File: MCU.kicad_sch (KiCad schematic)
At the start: 83 parts, among them J1 Conn_01x02_Pin, J11 Logger Connector, J12 UART Connector, J13 External UART, J14 External I2C, J15 JTAG Header, J2 Conn_01x02_Pin, J27 Conn_01x02_Pin, SW1 XRSn_button, U13 M24M01E-FMN6TP, U17 TRS3221EIPWR, U5 F280025PNS, Y2 H130B-16.000-18-3030-EXT-TR

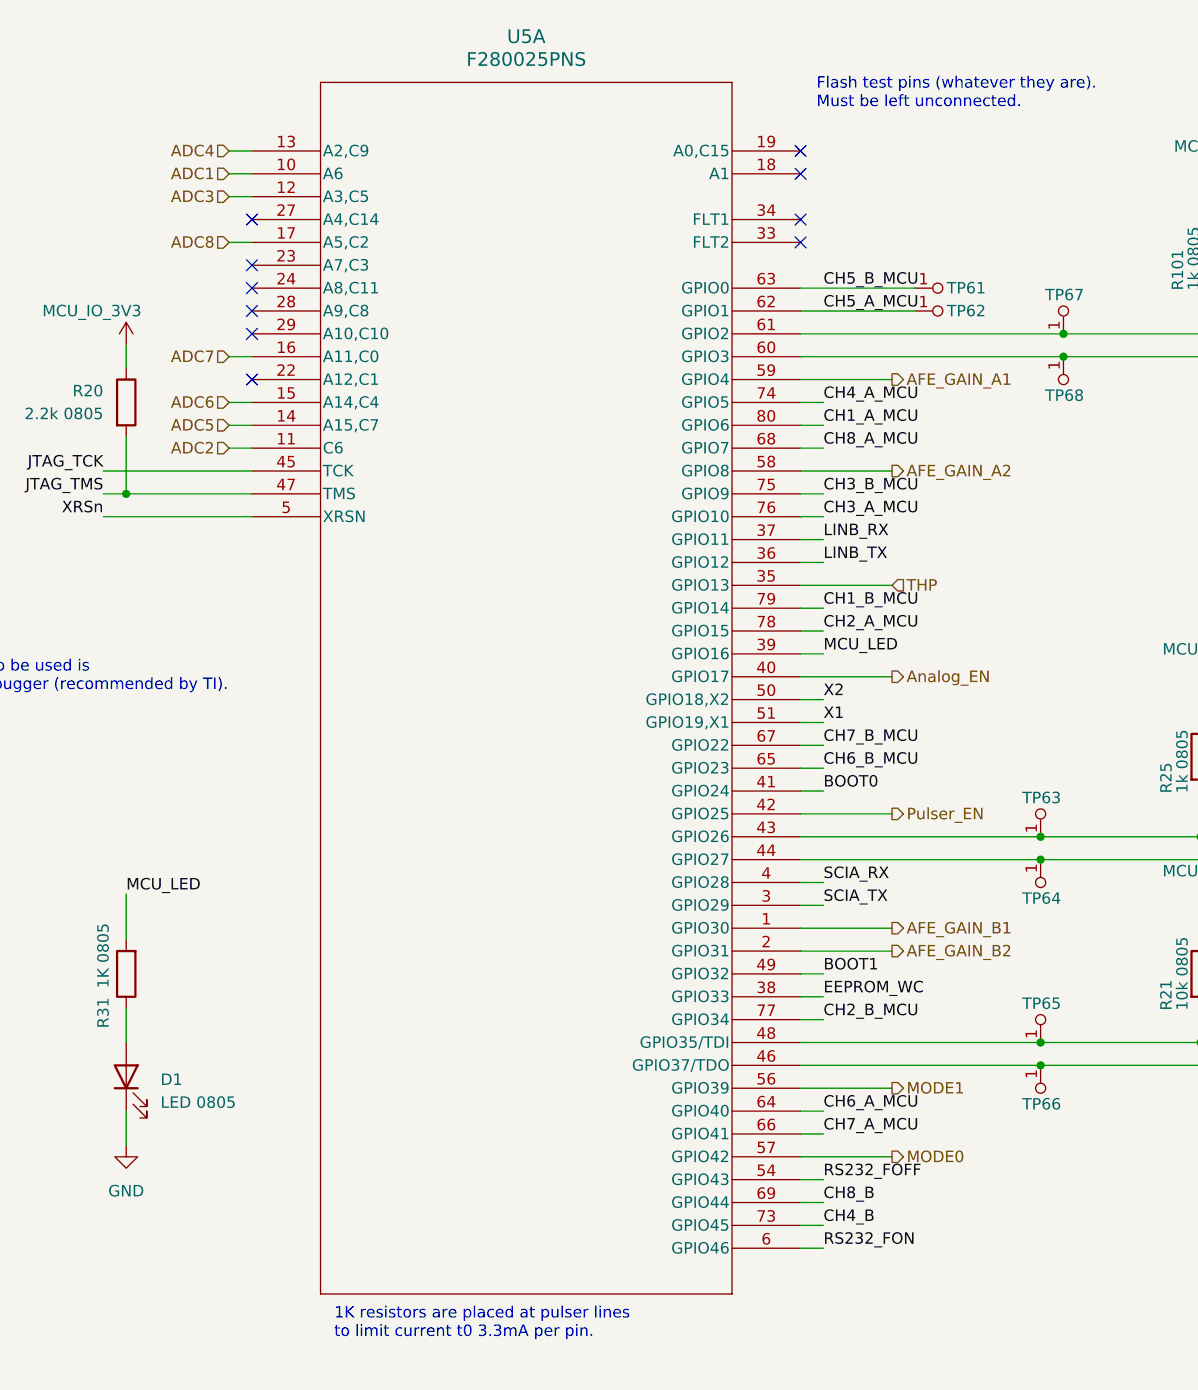
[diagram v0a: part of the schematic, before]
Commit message: Finished placement & started routing, check on stackup & see routing & sigal integrity videos downloaded
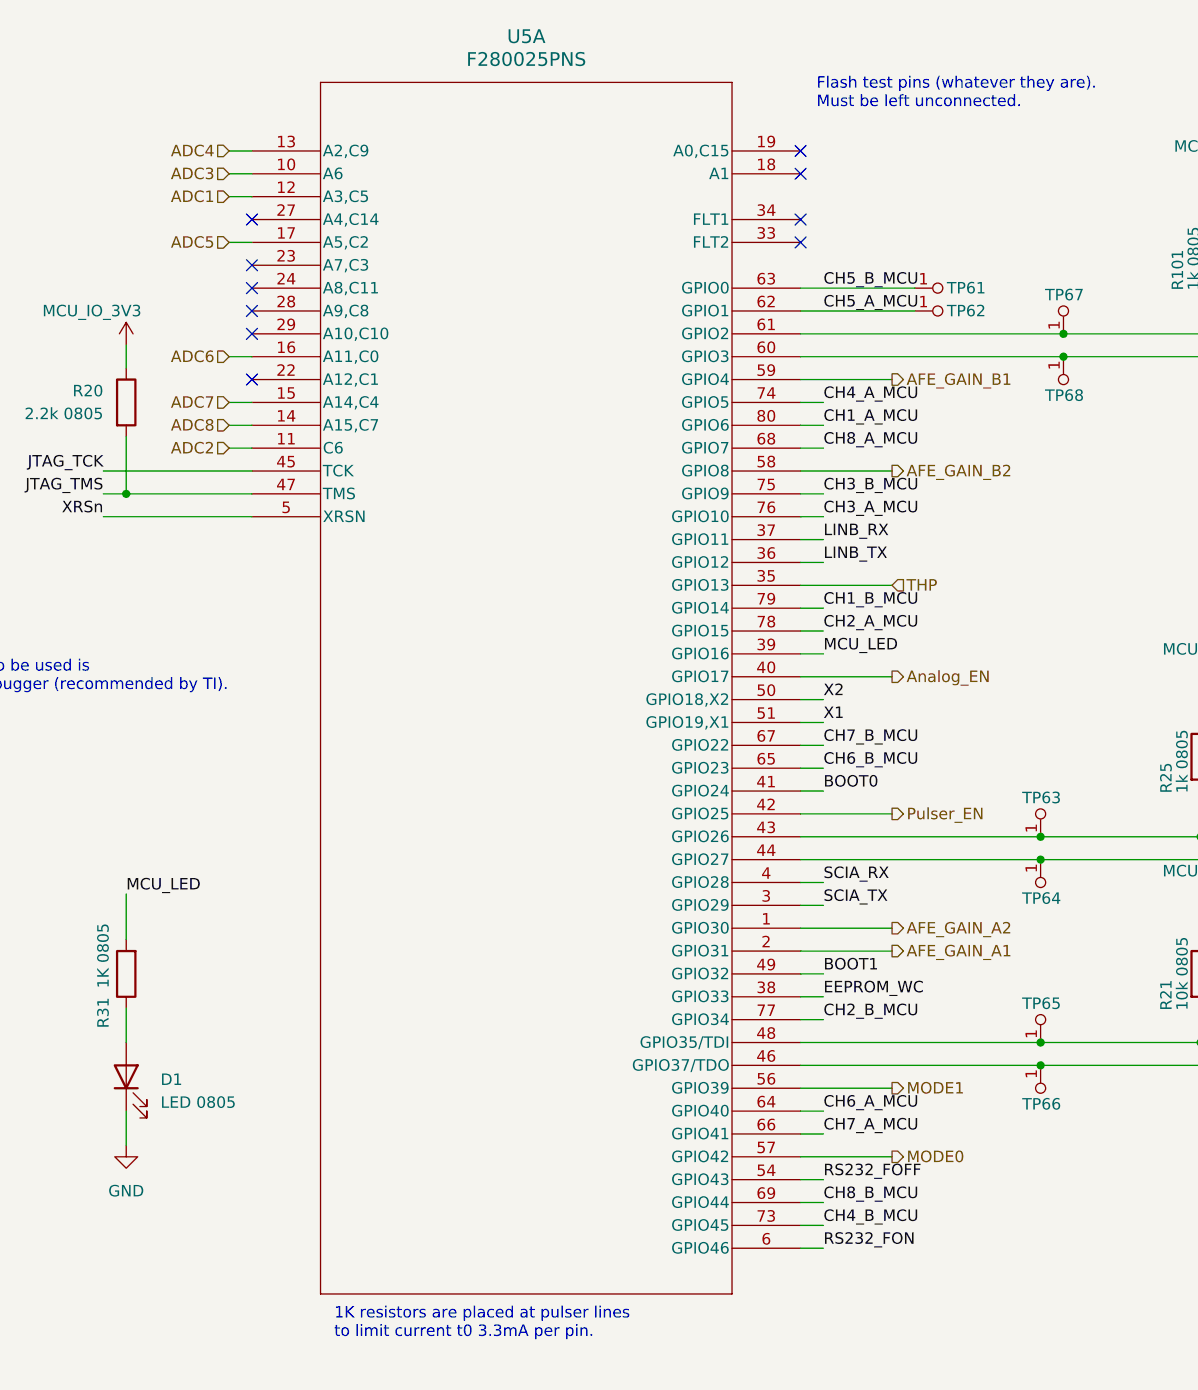
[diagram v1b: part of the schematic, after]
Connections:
- net ADC1: now also U5.12 (A3,C5); no longer U5.10 (A6)
- net ADC3: now also U5.10 (A6); no longer U5.12 (A3,C5)
- net ADC5: now also U5.17 (A5,C2); no longer U5.14 (A15,C7)
- net ADC6: now also U5.16 (A11,C0); no longer U5.15 (A14,C4)
- net ADC7: now also U5.15 (A14,C4); no longer U5.16 (A11,C0)
- net ADC8: now also U5.14 (A15,C7); no longer U5.17 (A5,C2)
- net AFE_GAIN_A1: now also U5.2 (GPIO31); no longer U5.59 (GPIO4)
- net AFE_GAIN_A2: now also U5.1 (GPIO30); no longer U5.58 (GPIO8)
- net AFE_GAIN_B1: now also U5.59 (GPIO4); no longer U5.1 (GPIO30)
- net AFE_GAIN_B2: now also U5.58 (GPIO8); no longer U5.2 (GPIO31)
- net CH4_B: no longer U5.73 (GPIO45)
- net CH4_B_MCU: now also U5.73 (GPIO45)
- net CH8_B: no longer U5.69 (GPIO44)
- net CH8_B_MCU: now also U5.69 (GPIO44)

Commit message: started routing, finished 15%
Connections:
- net JTAG_TCK: now also J15.6 (Pin_6); no longer J15.5 (Pin_5)
- net JTAG_TDO: now also J15.5 (Pin_5); no longer J15.4 (Pin_4)
- net JTAG_TMS: now also J15.4 (Pin_4); no longer J15.6 (Pin_6)
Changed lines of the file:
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@@
 	)
 	(label "JTAG_TDO"
-		(at 190.5 254 0)
+		(at 190.5 256.54 0)
 		(effects
 			(font
@@
 	)
 	(label "JTAG_TCK"
-		(at 190.5 256.54 0)
+		(at 190.5 259.08 0)
 		(effects
 			(font
@@
 	)
 	(label "JTAG_TMS"
-		(at 190.5 259.08 0)
-		(effects
-			(font
+		(at 190.5 254 0)
+		(effects
+			(font

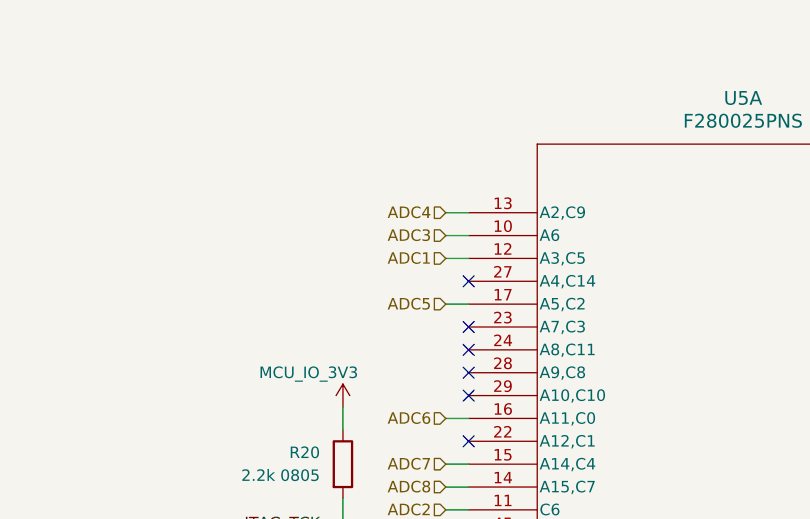
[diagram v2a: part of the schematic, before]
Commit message: Finished 70% fr this time, power planes are remaining and some minor connections to the AFE's power & cfg pins, dont forget xrst
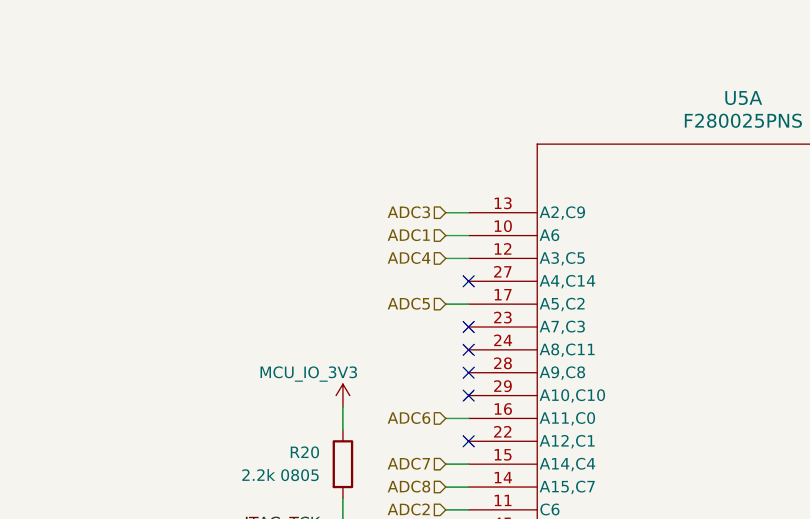
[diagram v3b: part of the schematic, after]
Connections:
- net ADC1: now also U5.10 (A6); no longer U5.12 (A3,C5)
- net ADC3: now also U5.13 (A2,C9); no longer U5.10 (A6)
- net ADC4: now also U5.12 (A3,C5); no longer U5.13 (A2,C9)

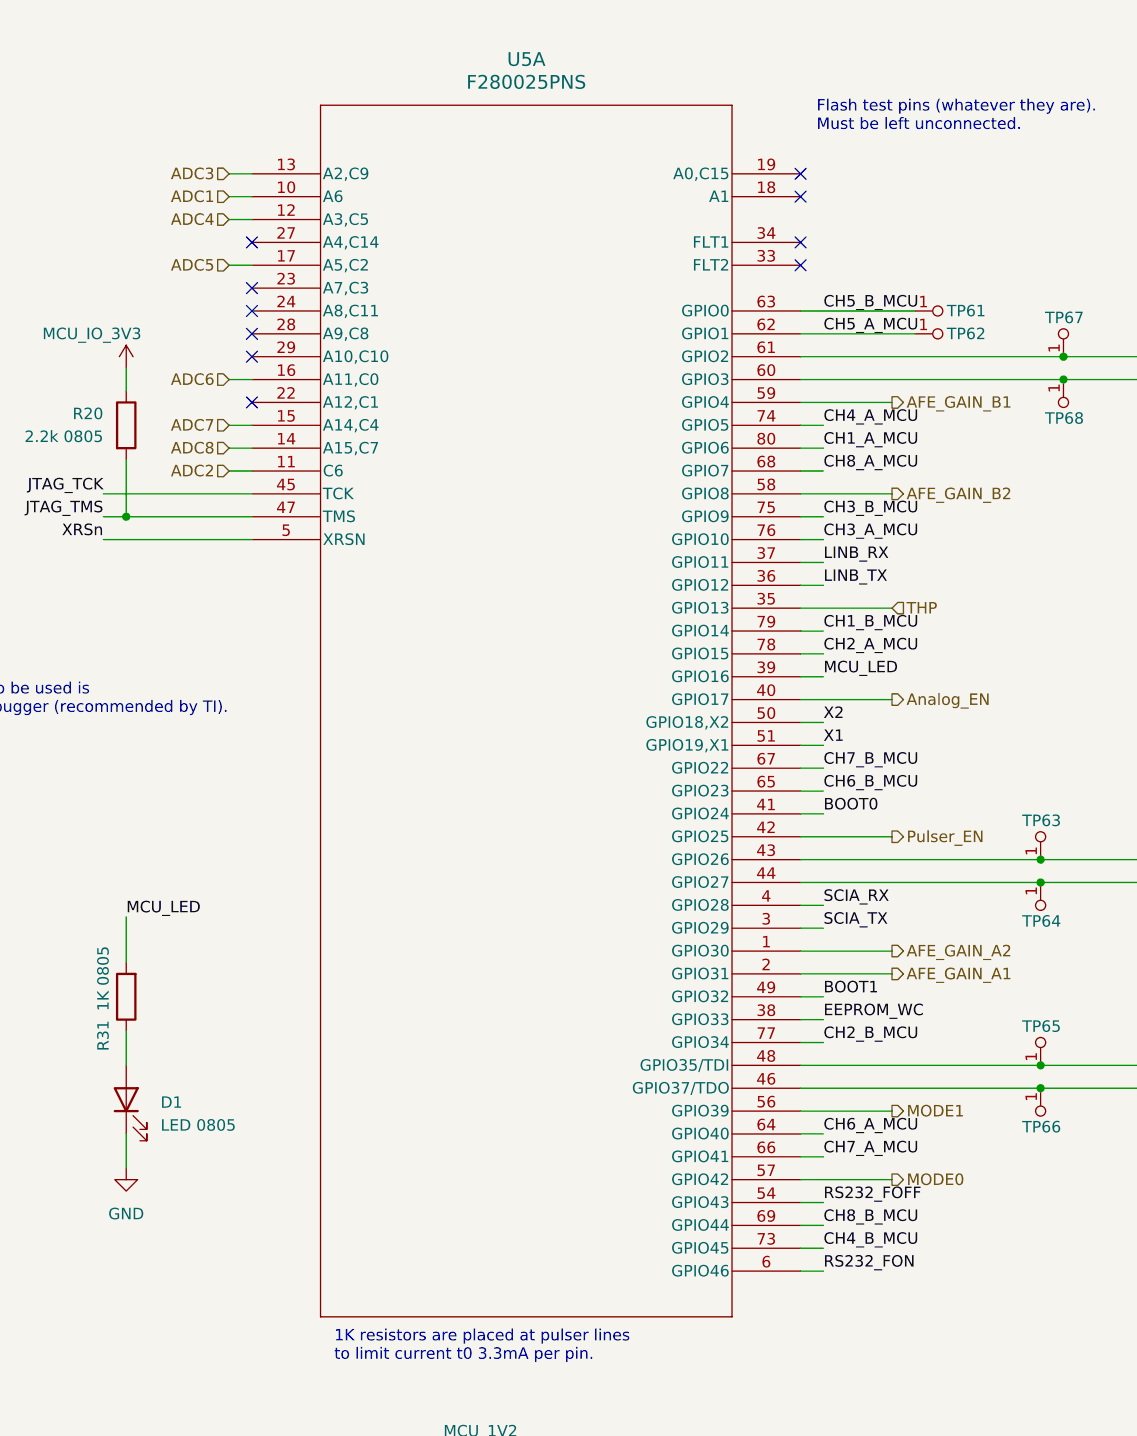
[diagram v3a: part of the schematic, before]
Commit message: 5% left, rearrange ADC channels for right AFE
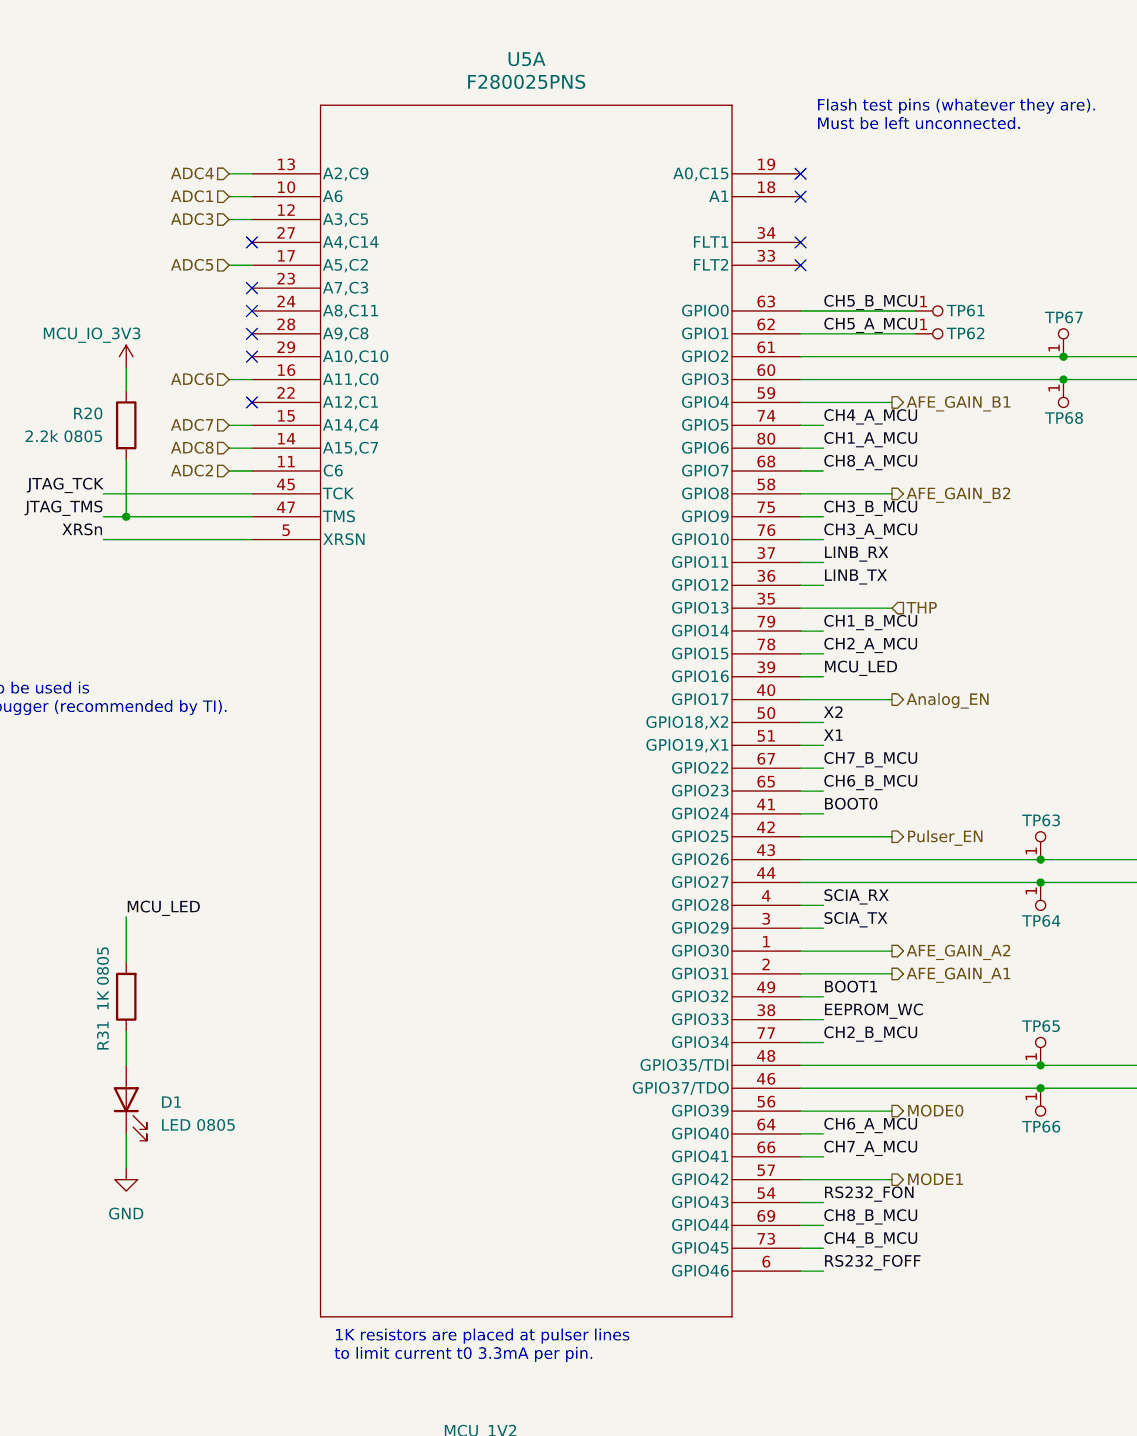
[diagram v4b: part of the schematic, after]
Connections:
- net ADC3: now also U5.12 (A3,C5); no longer U5.13 (A2,C9)
- net ADC4: now also U5.13 (A2,C9); no longer U5.12 (A3,C5)
- net MODE0: now also U5.56 (GPIO39); no longer U5.57 (GPIO42)
- net MODE1: now also U5.57 (GPIO42); no longer U5.56 (GPIO39)
- net RS232_FOFF: now also U5.6 (GPIO46); no longer U5.54 (GPIO43)
- net RS232_FON: now also U5.54 (GPIO43); no longer U5.6 (GPIO46)
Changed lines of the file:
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@@
 	)
 	(label "RS232_FOFF"
-		(at 309.88 148.59 0)
+		(at 309.88 156.21 0)
 		(effects
 			(font
@@
 	)
 	(label "RS232_FON"
-		(at 309.88 156.21 0)
+		(at 309.88 148.59 0)
 		(effects
 			(font
@@
 	(hierarchical_label "MODE0"
 		(shape output)
-		(at 317.5 146.05 0)
+		(at 317.5 138.43 0)
 		(effects
 			(font
@@
 	(hierarchical_label "MODE1"
 		(shape output)
-		(at 317.5 138.43 0)
+		(at 317.5 146.05 0)
 		(effects
 			(font
@@
 	(hierarchical_label "ADC3"
 		(shape input)
-		(at 243.84 34.29 180)
+		(at 243.84 39.37 180)
 		(effects
 			(font
@@
 	(hierarchical_label "ADC4"
 		(shape input)
-		(at 243.84 39.37 180)
-		(effects
-			(font
+		(at 243.84 34.29 180)
+		(effects
+			(font
